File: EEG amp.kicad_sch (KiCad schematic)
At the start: 31 parts, among them J1 Electrodes, J2 Power, J3 Output, J4 Status, U1 AD8232

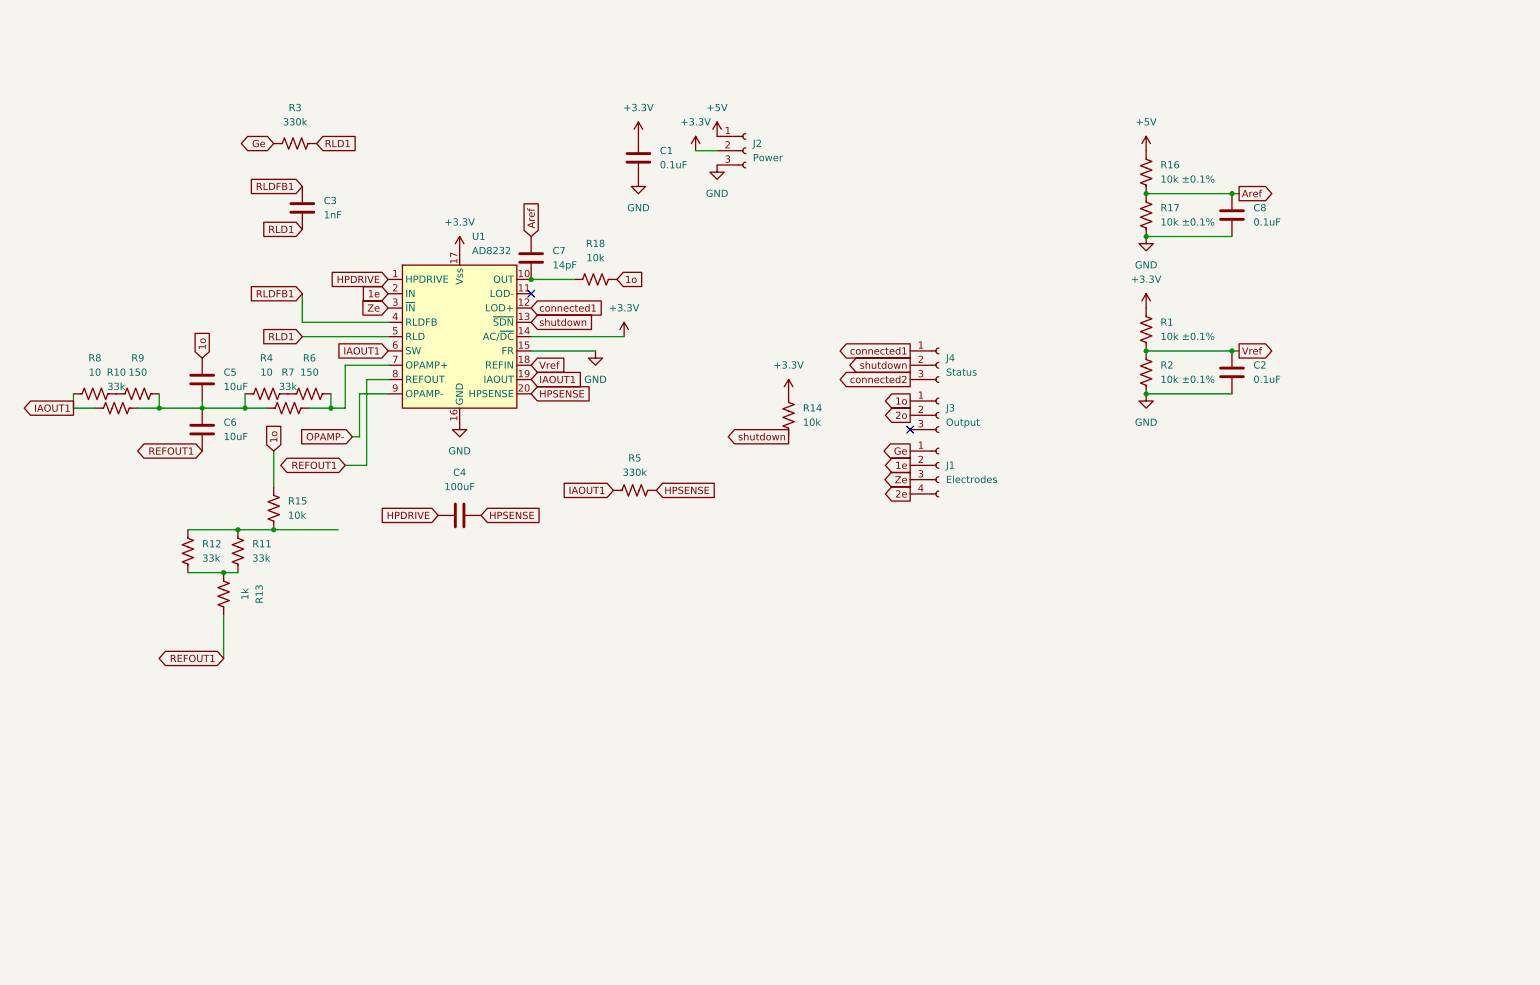
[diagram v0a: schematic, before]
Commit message: Organized and added mux
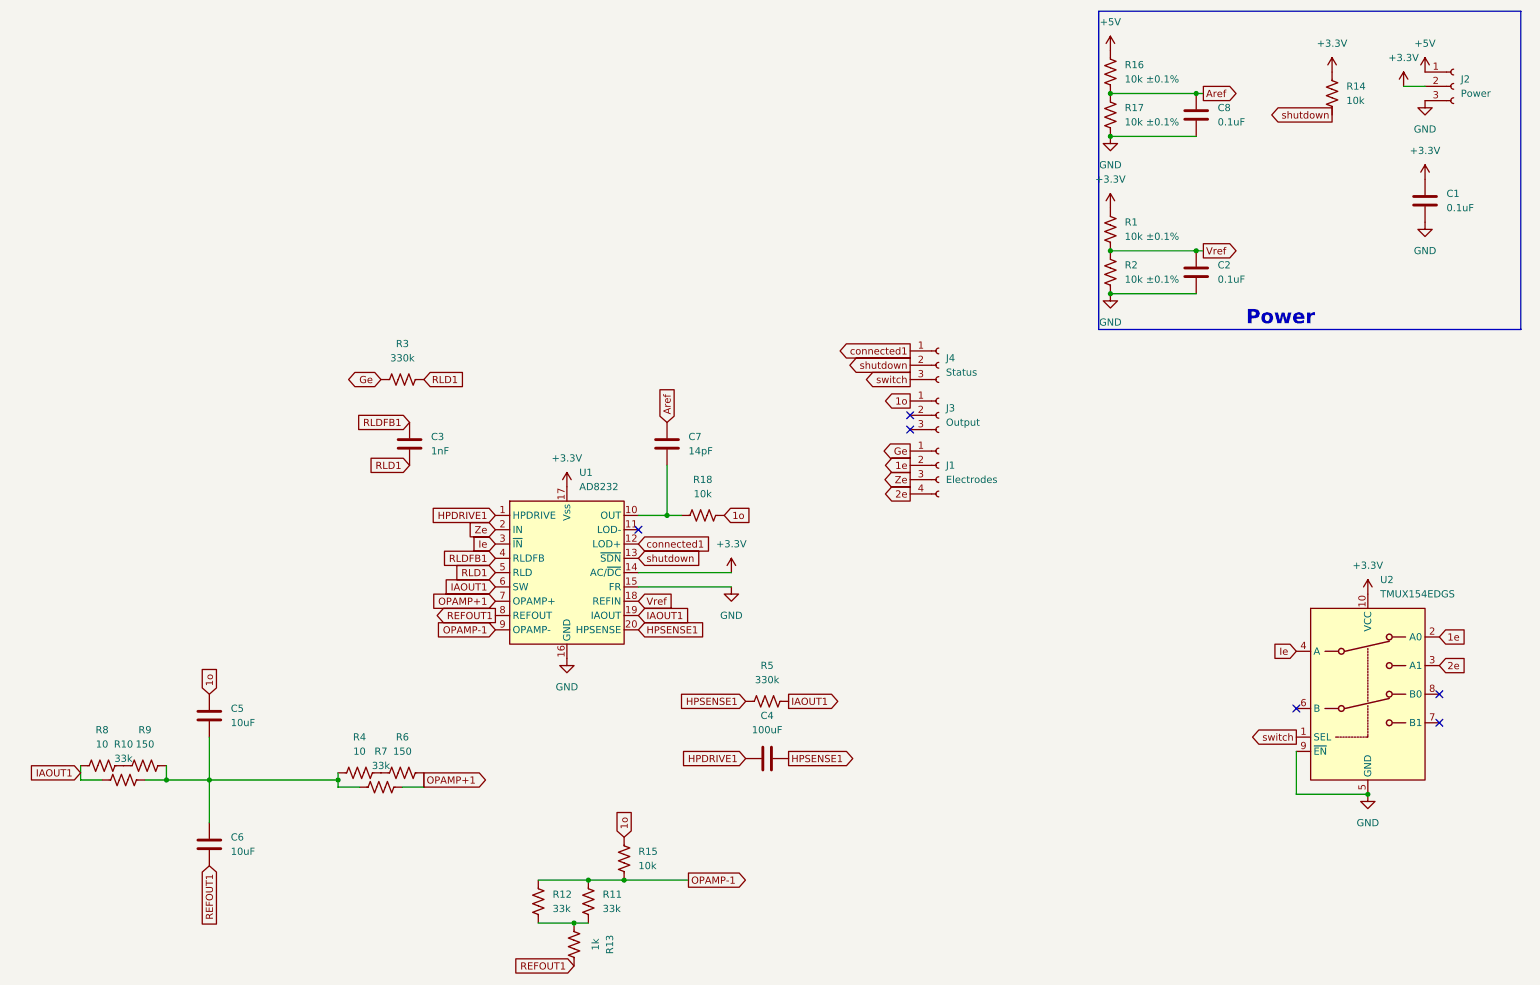
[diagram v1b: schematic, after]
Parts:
- added U2: TMUX154EDGS, Package_SO:VSSOP-10_3x3mm_P0.5mm, symbol Analog_Switch:TMUX154EDGS
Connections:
- net OPAMP- is gone; now on net OPAMP-1: U1.9 (OPAMP-)
- net +3.3V: now also U2.10 (VCC)
- net 1e: now also U2.2 (A0); no longer U1.2 (IN)
- net 2e: now also U2.3 (A1)
- net GND: now also U2.5 (GND), U2.9 (~{EN})
- net Ze: now also U1.2 (IN); no longer U1.3 (~{IN})
- net OPAMP-1: now reaches R11.1, R12.1, R15.2
- net OPAMP+1: now reaches R6.2, R7.2, U1.7 (OPAMP+)
- net 2o: no longer names the net of J3.2 (Pin_2)
- net HPDRIVE renamed HPDRIVE1
- net HPSENSE renamed HPSENSE1
- net connected2 renamed switch
- net switch: now also U2.1 (SEL)
- new net Ie: U1.3 (~{IN}), U2.4 (A)
- no-connect marks 2 -> 6
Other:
- note added: "Power"
- moved on the sheet: C1, C2, C3, C4, C5, C6, C7, C8, J2, R1, R10, R11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

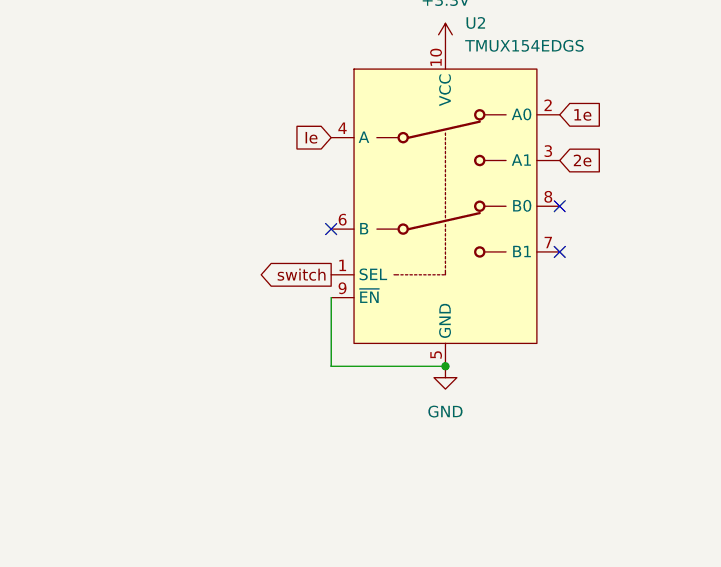
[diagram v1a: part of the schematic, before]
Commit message: added lock files to gitignore and changed the mux a bit
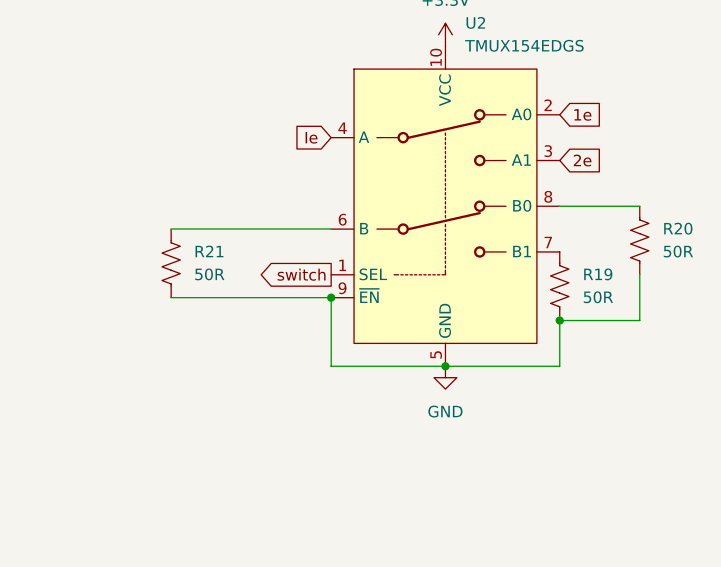
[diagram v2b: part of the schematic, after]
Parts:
- added R19, R20, R21: 50R, Resistor_SMD:R_0402_1005Metric, symbol Device:R_US
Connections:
- net GND: now also R19.2, R20.2, R21.2
- net at U2.6 (B): now also R21.1
- net at U2.7 (B1): now also R19.1
- net at U2.8 (B0): now also R20.1
- no-connect marks 6 -> 3

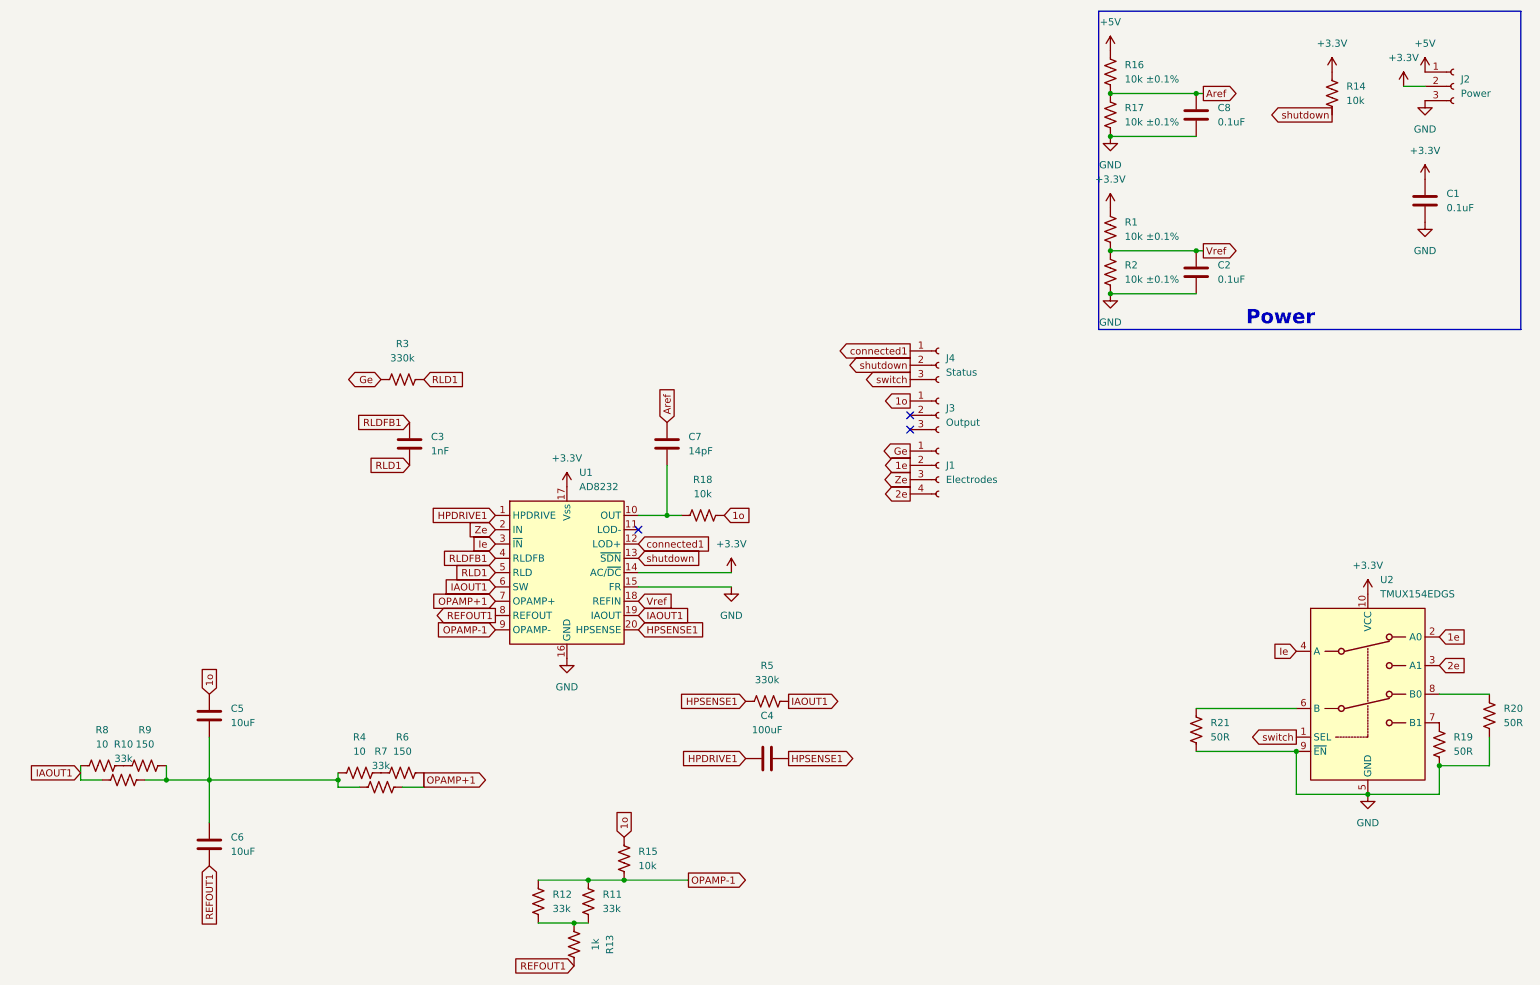
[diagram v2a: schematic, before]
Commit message: Organization and status LEDs
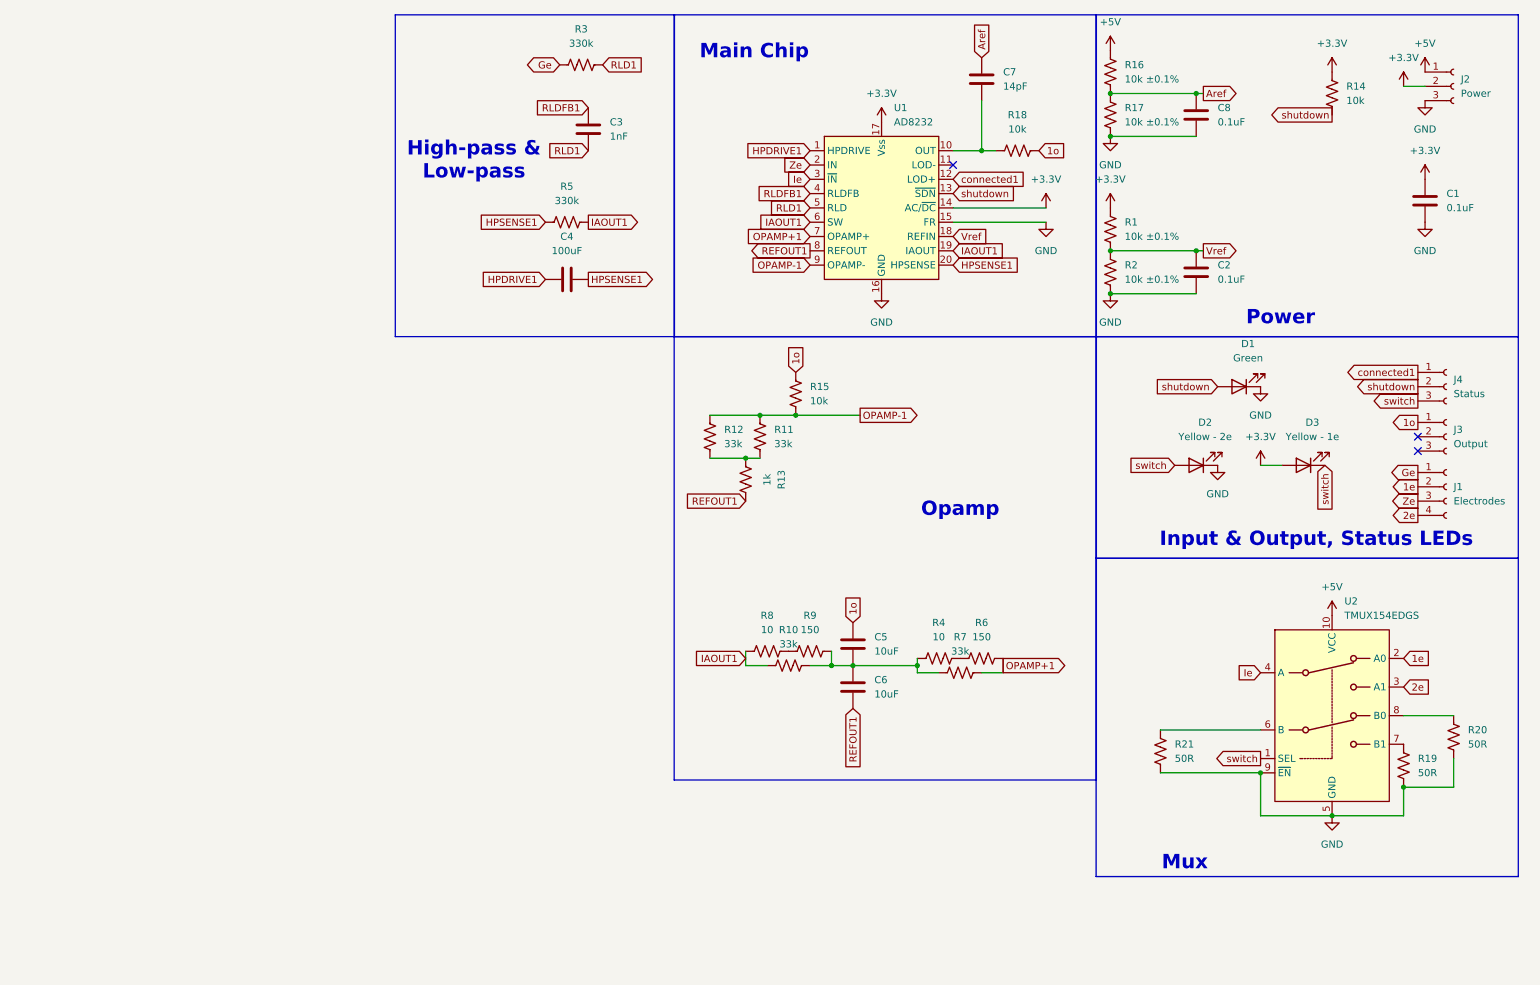
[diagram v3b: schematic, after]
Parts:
- added D1: Green, LED_THT:LED_D5.0mm, symbol Device:LED
- added D2: Yellow - 2e, LED_THT:LED_D5.0mm, symbol Device:LED
- added D3: Yellow - 1e, LED_THT:LED_D5.0mm, symbol Device:LED
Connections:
- net +3.3V: now also D3.2 (A); no longer U2.10 (VCC)
- net +5V: now also U2.10 (VCC)
- net GND: now also D1.1 (K), D2.1 (K)
- net shutdown: now also D1.2 (A)
- net switch: now also D2.2 (A), D3.1 (K)
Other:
- note added: "High-pass & Low-pass"
- note added: "Input & Output, Status LEDs"
- note added: "Main Chip"
- note added: "Mux"
- note added: "Opamp"
- moved on the sheet: C3, C4, C5, C6, C7, J1, J3, J4, R10, R11, R12, R13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
